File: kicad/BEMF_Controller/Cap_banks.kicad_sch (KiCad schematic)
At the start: 60 parts

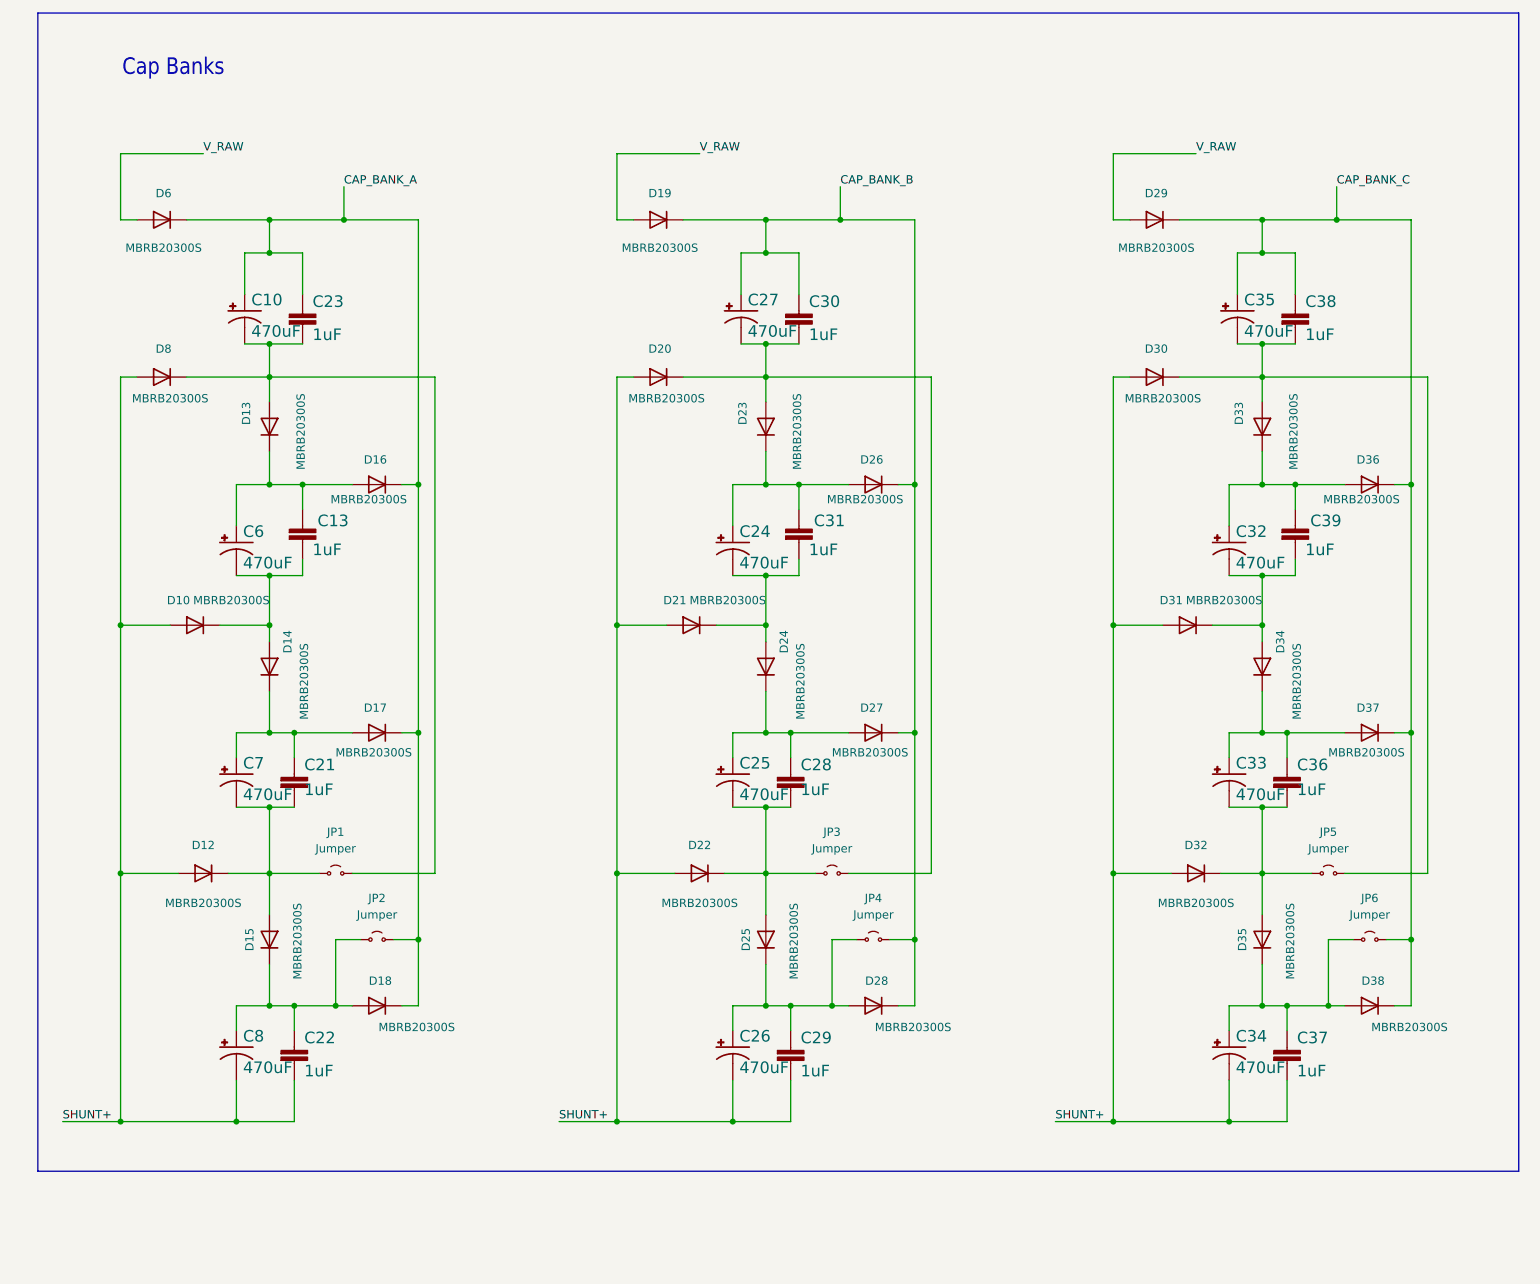
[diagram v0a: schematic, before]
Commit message: replaced shottky diodes
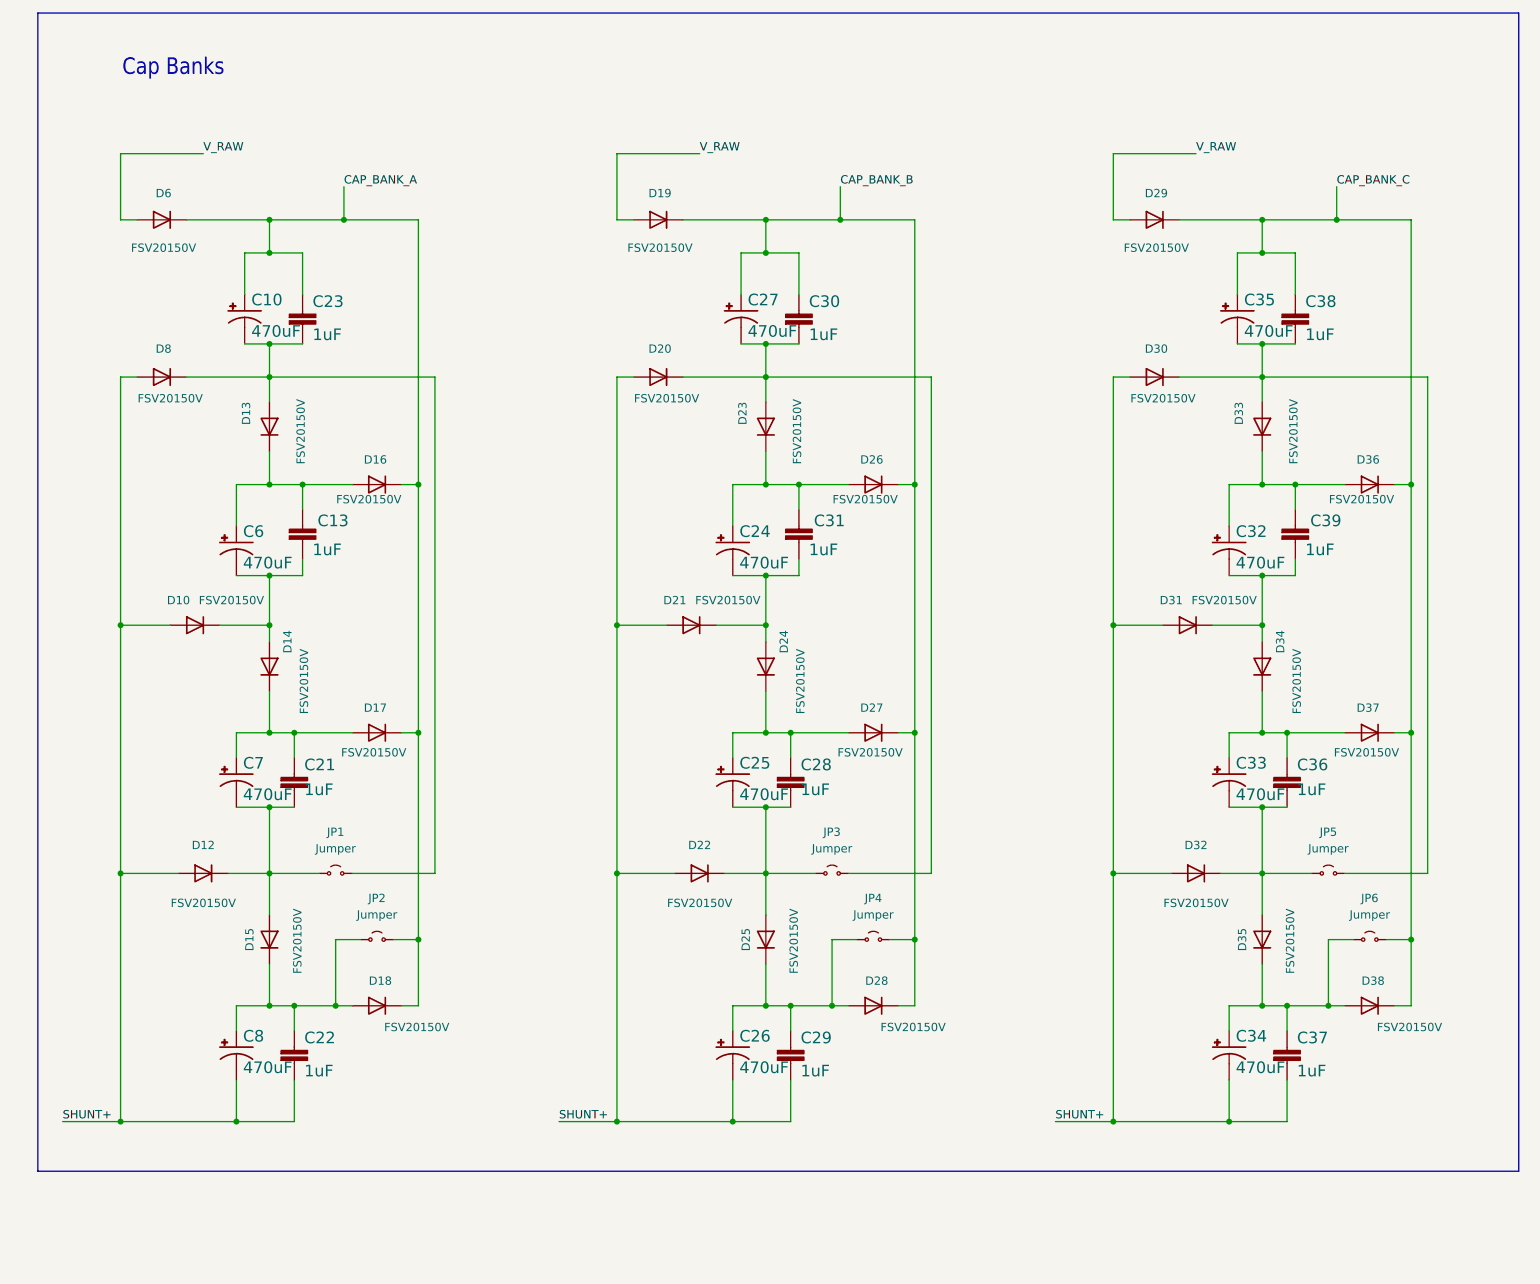
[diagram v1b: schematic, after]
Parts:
- D10, D12, D13, D14, D15, D16, D17, D18, D19, D20, D21, D22, D23, D24, D25, D26, D27, D28, D29, D30, D31, D32, D33, D34, D35, D36, D37, D38, D6, D8: value MBRB20300S -> FSV20150V; footprint Package_TO_SOT_SMD:TO-263-2 -> Package_TO_SOT_SMD:TO-277A
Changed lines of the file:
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@@
 			)
 		)
-		(property "Value" "MBRB20300S"
+		(property "Value" "FSV20150V"
 			(at 125.984 107.696 0)
 			(effects
@@
 			)
 		)
-		(property "Footprint" "Package_TO_SOT_SMD:TO-263-2"
+		(property "Footprint" "Package_TO_SOT_SMD:TO-277A"
 			(at 120.65 105.41 0)
 			(effects
@@
 			)
 		)
-		(property "Value" "MBRB20300S"
+		(property "Value" "FSV20150V"
 			(at 59.69 79.756 0)
 			(effects
@@
 			)
 		)
-		(property "Footprint" "Package_TO_SOT_SMD:TO-263-2"
+		(property "Footprint" "Package_TO_SOT_SMD:TO-277A"
 			(at 60.96 77.47 0)
 			(effects
@@
 			)
 		)
-		(property "Value" "MBRB20300S"
+		(property "Value" "FSV20150V"
 			(at 49.276 69.342 0)
 			(effects
@@
 			)
 		)
-		(property "Footprint" "Package_TO_SOT_SMD:TO-263-2"
+		(property "Footprint" "Package_TO_SOT_SMD:TO-277A"
 			(at 44.45 68.58 0)
 			(effects
@@
 			)
 		)
-		(property "Value" "MBRB20300S"
+		(property "Value" "FSV20150V"
 			(at 124.968 147.574 0)
 			(effects
@@
 			)
 		)
-		(property "Footprint" "Package_TO_SOT_SMD:TO-263-2"
+		(property "Footprint" "Package_TO_SOT_SMD:TO-277A"
 			(at 120.65 147.32 0)
 			(effects
@@
 			)
 		)
-		(property "Value" "MBRB20300S"
+		(property "Value" "FSV20150V"
 			(at 48.768 147.574 0)
 			(effects
@@
 			)
 		)
-		(property "Footprint" "Package_TO_SOT_SMD:TO-263-2"
+		(property "Footprint" "Package_TO_SOT_SMD:TO-277A"
 			(at 44.45 147.32 0)
 			(effects
@@
 			)
 		)
-		(property "Value" "MBRB20300S"
+		(property "Value" "FSV20150V"
 			(at 104.394 41.148 0)
 			(effects
@@
 			)
 		)
-		(property "Footprint" "Package_TO_SOT_SMD:TO-263-2"
+		(property "Footprint" "Package_TO_SOT_SMD:TO-277A"
 			(at 104.14 36.83 0)
 			(effects
@@
 			)
 		)
-		(property "Value" "MBRB20300S"
+		(property "Value" "FSV20150V"
 			(at 219.456 160.782 0)
 			(effects
@@
 			)
 		)
-		(property "Footprint" "Package_TO_SOT_SMD:TO-263-2"
+		(property "Footprint" "Package_TO_SOT_SMD:TO-277A"
 			(at 213.36 157.48 0)
 			(effects
@@
 			)
 		)
-		(property "Value" "MBRB20300S"
+		(property "Value" "FSV20150V"
 			(at 38.608 95.25 0)
 			(effects
@@
 			)
 		)
-		(property "Footprint" "Package_TO_SOT_SMD:TO-263-2"
+		(property "Footprint" "Package_TO_SOT_SMD:TO-277A"
 			(at 33.02 99.06 0)
 			(effects
@@
 			)
 		)
-		(property "Value" "MBRB20300S"
+		(property "Value" "FSV20150V"
 			(at 110.49 141.732 0)
 			(effects
@@
 			)
 		)
-		(property "Footprint" "Package_TO_SOT_SMD:TO-263-2"
+		(property "Footprint" "Package_TO_SOT_SMD:TO-277A"
 			(at 110.49 137.16 0)
 			(effects
@@
 			)
 		)
-		(property "Value" "MBRB20300S"
+		(property "Value" "FSV20150V"
 			(at 201.676 69.342 0)
 			(effects
@@
 			)
 		)
-		(property "Footprint" "Package_TO_SOT_SMD:TO-263-2"
+		(property "Footprint" "Package_TO_SOT_SMD:TO-277A"
 			(at 196.85 68.58 0)
 			(effects
@@
 			)
 		)
-		(property "Value" "MBRB20300S"
+		(property "Value" "FSV20150V"
 			(at 125.476 69.342 0)
 			(effects
@@
 			)
 		)
-		(property "Footprint" "Package_TO_SOT_SMD:TO-263-2"
+		(property "Footprint" "Package_TO_SOT_SMD:TO-277A"
 			(at 120.65 68.58 0)
 			(effects
@@
 			)
 		)
-		(property "Value" "MBRB20300S"
+		(property "Value" "FSV20150V"
 			(at 49.784 107.696 0)
 			(effects
@@
 			)
 		)
-		(property "Footprint" "Package_TO_SOT_SMD:TO-263-2"
+		(property "Footprint" "Package_TO_SOT_SMD:TO-277A"
 			(at 44.45 105.41 0)
 			(effects
@@
 			)
 		)
-		(property "Value" "MBRB20300S"
+		(property "Value" "FSV20150V"
 			(at 135.89 79.756 0)
 			(effects
@@
 			)
 		)
-		(property "Footprint" "Package_TO_SOT_SMD:TO-263-2"
+		(property "Footprint" "Package_TO_SOT_SMD:TO-277A"
 			(at 137.16 77.47 0)
 			(effects
@@
 			)
 		)
-		(property "Value" "MBRB20300S"
+		(property "Value" "FSV20150V"
 			(at 181.61 64.262 0)
 			(effects
@@
 			)
 		)
-		(property "Footprint" "Package_TO_SOT_SMD:TO-263-2"
+		(property "Footprint" "Package_TO_SOT_SMD:TO-277A"
 			(at 180.34 60.96 0)
 			(effects
@@
 			)
 		)
-		(property "Value" "MBRB20300S"
+		(property "Value" "FSV20150V"
 			(at 136.652 118.618 0)
 			(effects
@@
 			)
 		)
-		(property "Footprint" "Package_TO_SOT_SMD:TO-263-2"
+		(property "Footprint" "Package_TO_SOT_SMD:TO-277A"
 			(at 137.16 115.57 0)
 			(effects
@@
 			)
 		)
-		(property "Value" "MBRB20300S"
+		(property "Value" "FSV20150V"
 			(at 60.452 118.618 0)
 			(effects
@@
 			)
 		)
-		(property "Footprint" "Package_TO_SOT_SMD:TO-263-2"
+		(property "Footprint" "Package_TO_SOT_SMD:TO-277A"
 			(at 60.96 115.57 0)
 			(effects
@@
 			)
 		)
-		(property "Value" "MBRB20300S"
+		(property "Value" "FSV20150V"
 			(at 202.184 107.696 0)
 			(effects
@@
 			)
 		)
-		(property "Footprint" "Package_TO_SOT_SMD:TO-263-2"
+		(property "Footprint" "Package_TO_SOT_SMD:TO-277A"
 			(at 196.85 105.41 0)
 			(effects
@@
 			)
 		)
-		(property "Value" "MBRB20300S"
+		(property "Value" "FSV20150V"
 			(at 67.056 160.782 0)
 			(effects
@@
 			)
 		)
-		(property "Footprint" "Package_TO_SOT_SMD:TO-263-2"
+		(property "Footprint" "Package_TO_SOT_SMD:TO-277A"
 			(at 60.96 157.48 0)
 			(effects
@@
 			)
 		)
-		(property "Value" "MBRB20300S"
+		(property "Value" "FSV20150V"
 			(at 186.69 141.732 0)
 			(effects
@@
 			)
 		)
-		(property "Footprint" "Package_TO_SOT_SMD:TO-263-2"
+		(property "Footprint" "Package_TO_SOT_SMD:TO-277A"
 			(at 186.69 137.16 0)
 			(effects
@@
 			)
 		)
-		(property "Value" "MBRB20300S"
+		(property "Value" "FSV20150V"
 			(at 191.008 95.25 0)
 			(effects
@@
 			)
 		)
-		(property "Footprint" "Package_TO_SOT_SMD:TO-263-2"
+		(property "Footprint" "Package_TO_SOT_SMD:TO-277A"
 			(at 185.42 99.06 0)
 			(effects
@@
 			)
 		)
-		(property "Value" "MBRB20300S"
+		(property "Value" "FSV20150V"
 			(at 28.194 41.148 0)
 			(effects
@@
 			)
 		)
-		(property "Footprint" "Package_TO_SOT_SMD:TO-263-2"
+		(property "Footprint" "Package_TO_SOT_SMD:TO-277A"
 			(at 27.94 36.83 0)
 			(effects
@@
 			)
 		)
-		(property "Value" "MBRB20300S"
+		(property "Value" "FSV20150V"
 			(at 105.41 64.262 0)
 			(effects
@@
 			)
 		)
-		(property "Footprint" "Package_TO_SOT_SMD:TO-263-2"
+		(property "Footprint" "Package_TO_SOT_SMD:TO-277A"
 			(at 104.14 60.96 0)
 			(effects
@@
 			)
 		)
-		(property "Value" "MBRB20300S"
+		(property "Value" "FSV20150V"
 			(at 180.594 41.148 0)
 			(effects
@@
 			)
 		)
-		(property "Footprint" "Package_TO_SOT_SMD:TO-263-2"
+		(property "Footprint" "Package_TO_SOT_SMD:TO-277A"
 			(at 180.34 36.83 0)
 			(effects
@@
 			)
 		)
-		(property "Value" "MBRB20300S"
+		(property "Value" "FSV20150V"
 			(at 212.852 118.618 0)
 			(effects
@@
 			)
 		)
-		(property "Footprint" "Package_TO_SOT_SMD:TO-263-2"
+		(property "Footprint" "Package_TO_SOT_SMD:TO-277A"
 			(at 213.36 115.57 0)
 			(effects
@@
 			)
 		)
-		(property "Value" "MBRB20300S"
+		(property "Value" "FSV20150V"
 			(at 34.29 141.732 0)
 			(effects
@@
 			)
 		)
-		(property "Footprint" "Package_TO_SOT_SMD:TO-263-2"
+		(property "Footprint" "Package_TO_SOT_SMD:TO-277A"
 			(at 34.29 137.16 0)
 			(effects
@@
 			)
 		)
-		(property "Value" "MBRB20300S"
+		(property "Value" "FSV20150V"
 			(at 29.21 64.262 0)
 			(effects
@@
 			)
 		)
-		(property "Footprint" "Package_TO_SOT_SMD:TO-263-2"
+		(property "Footprint" "Package_TO_SOT_SMD:TO-277A"
 			(at 27.94 60.96 0)
 			(effects
@@
 			)
 		)
-		(property "Value" "MBRB20300S"
+		(property "Value" "FSV20150V"
 			(at 212.09 79.756 0)
 			(effects
@@
 			)
 		)
-		(property "Footprint" "Package_TO_SOT_SMD:TO-263-2"
+		(property "Footprint" "Package_TO_SOT_SMD:TO-277A"
 			(at 213.36 77.47 0)
 			(effects
@@
 			)
 		)
-		(property "Value" "MBRB20300S"
+		(property "Value" "FSV20150V"
 			(at 114.808 95.25 0)
 			(effects
@@
 			)
 		)
-		(property "Footprint" "Package_TO_SOT_SMD:TO-263-2"
+		(property "Footprint" "Package_TO_SOT_SMD:TO-277A"
 			(at 109.22 99.06 0)
 			(effects
@@
 			)
 		)
-		(property "Value" "MBRB20300S"
+		(property "Value" "FSV20150V"
 			(at 201.168 147.574 0)
 			(effects
@@
 			)
 		)
-		(property "Footprint" "Package_TO_SOT_SMD:TO-263-2"
+		(property "Footprint" "Package_TO_SOT_SMD:TO-277A"
 			(at 196.85 147.32 0)
 			(effects
@@
 			)
 		)
-		(property "Value" "MBRB20300S"
+		(property "Value" "FSV20150V"
 			(at 143.256 160.782 0)
 			(effects
@@
 			)
 		)
-		(property "Footprint" "Package_TO_SOT_SMD:TO-263-2"
+		(property "Footprint" "Package_TO_SOT_SMD:TO-277A"
 			(at 137.16 157.48 0)
 			(effects

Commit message: Adapted footprint for capacitors.
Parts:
- C10, C24, C25, C26, C27, C32, C33, C34, C35, C6, C7, C8: footprint Capacitor_THT:CP_Radial_D10.0mm_P5.00mm -> main:CPOL-RADIAL-5MM-10MM
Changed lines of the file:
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@@
 			)
 		)
-		(property "Footprint" "Capacitor_THT:CP_Radial_D10.0mm_P5.00mm"
+		(property "Footprint" "main:CPOL-RADIAL-5MM-10MM"
 			(at 39.37 163.83 0)
 			(effects
@@
 			)
 		)
-		(property "Footprint" "Capacitor_THT:CP_Radial_D10.0mm_P5.00mm"
+		(property "Footprint" "main:CPOL-RADIAL-5MM-10MM"
 			(at 116.84 50.8 0)
 			(effects
@@
 			)
 		)
-		(property "Footprint" "Capacitor_THT:CP_Radial_D10.0mm_P5.00mm"
+		(property "Footprint" "main:CPOL-RADIAL-5MM-10MM"
 			(at 191.77 163.83 0)
 			(effects
@@
 			)
 		)
-		(property "Footprint" "Capacitor_THT:CP_Radial_D10.0mm_P5.00mm"
+		(property "Footprint" "main:CPOL-RADIAL-5MM-10MM"
 			(at 191.77 121.92 0)
 			(effects
@@
 			)
 		)
-		(property "Footprint" "Capacitor_THT:CP_Radial_D10.0mm_P5.00mm"
+		(property "Footprint" "main:CPOL-RADIAL-5MM-10MM"
 			(at 39.37 86.36 0)
 			(effects
@@
 			)
 		)
-		(property "Footprint" "Capacitor_THT:CP_Radial_D10.0mm_P5.00mm"
+		(property "Footprint" "main:CPOL-RADIAL-5MM-10MM"
 			(at 115.57 86.36 0)
 			(effects
@@
 			)
 		)
-		(property "Footprint" "Capacitor_THT:CP_Radial_D10.0mm_P5.00mm"
+		(property "Footprint" "main:CPOL-RADIAL-5MM-10MM"
 			(at 115.57 163.83 0)
 			(effects
@@
 			)
 		)
-		(property "Footprint" "Capacitor_THT:CP_Radial_D10.0mm_P5.00mm"
+		(property "Footprint" "main:CPOL-RADIAL-5MM-10MM"
 			(at 193.04 50.8 0)
 			(effects
@@
 			)
 		)
-		(property "Footprint" "Capacitor_THT:CP_Radial_D10.0mm_P5.00mm"
+		(property "Footprint" "main:CPOL-RADIAL-5MM-10MM"
 			(at 115.57 121.92 0)
 			(effects
@@
 			)
 		)
-		(property "Footprint" "Capacitor_THT:CP_Radial_D10.0mm_P5.00mm"
+		(property "Footprint" "main:CPOL-RADIAL-5MM-10MM"
 			(at 40.64 50.8 0)
 			(effects
@@
 			)
 		)
-		(property "Footprint" "Capacitor_THT:CP_Radial_D10.0mm_P5.00mm"
+		(property "Footprint" "main:CPOL-RADIAL-5MM-10MM"
 			(at 191.77 86.36 0)
 			(effects
@@
 			)
 		)
-		(property "Footprint" "Capacitor_THT:CP_Radial_D10.0mm_P5.00mm"
+		(property "Footprint" "main:CPOL-RADIAL-5MM-10MM"
 			(at 39.37 121.92 0)
 			(effects

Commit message: Change to mosfets.
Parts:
- JP1, JP2, JP3, JP4, JP5, JP6: footprint Connector_PinHeader_2.54mm:PinHeader_1x02_P2.54mm_Vertical -> Jumper:SolderJumper-2_P1.3mm_Open_RoundedPad1.0x1.5mm
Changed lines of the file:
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@@
 			)
 		)
-		(property "Footprint" "Connector_PinHeader_2.54mm:PinHeader_1x02_P2.54mm_Vertical"
+		(property "Footprint" "Jumper:SolderJumper-2_P1.3mm_Open_RoundedPad1.0x1.5mm"
 			(at 213.36 147.32 0)
 			(effects
@@
 			)
 		)
-		(property "Footprint" "Connector_PinHeader_2.54mm:PinHeader_1x02_P2.54mm_Vertical"
+		(property "Footprint" "Jumper:SolderJumper-2_P1.3mm_Open_RoundedPad1.0x1.5mm"
 			(at 130.81 137.16 0)
 			(effects
@@
 			)
 		)
-		(property "Footprint" "Connector_PinHeader_2.54mm:PinHeader_1x02_P2.54mm_Vertical"
+		(property "Footprint" "Jumper:SolderJumper-2_P1.3mm_Open_RoundedPad1.0x1.5mm"
 			(at 137.16 147.32 0)
 			(effects
@@
 			)
 		)
-		(property "Footprint" "Connector_PinHeader_2.54mm:PinHeader_1x02_P2.54mm_Vertical"
+		(property "Footprint" "Jumper:SolderJumper-2_P1.3mm_Open_RoundedPad1.0x1.5mm"
 			(at 60.96 147.32 0)
 			(effects
@@
 			)
 		)
-		(property "Footprint" "Connector_PinHeader_2.54mm:PinHeader_1x02_P2.54mm_Vertical"
+		(property "Footprint" "Jumper:SolderJumper-2_P1.3mm_Open_RoundedPad1.0x1.5mm"
 			(at 54.61 137.16 0)
 			(effects
@@
 			)
 		)
-		(property "Footprint" "Connector_PinHeader_2.54mm:PinHeader_1x02_P2.54mm_Vertical"
+		(property "Footprint" "Jumper:SolderJumper-2_P1.3mm_Open_RoundedPad1.0x1.5mm"
 			(at 207.01 137.16 0)
 			(effects
